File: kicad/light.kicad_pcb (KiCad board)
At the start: 4 copper layers, 58 x 40 mm, 138 parts, among them J2 USB_C_Receptacle_USB2.0_16P, J3 Barrell Jack, J4 01x04, J5 SM03B-SRSS-TB, J6 SM03B-SRSS-TB, J9 Conn_01x09_MountingPin, Q1 NMOS, Q2 NMOS, Q3 NMOS, SW1 Boot, SW3 On/Off, SW4 Mode, U1 RP2350A-QFN60, U10 MAX6816, U2 TPS5405DR, U3 W25Q128JVS, U4 LBEE5KL1YN-814, U5 TPS2115ADRBR, U6 TPS2115ADRBR, U7 HDC1080, U8 MAX6816, U9 MAX6816, Y1 ABM8-272-T3

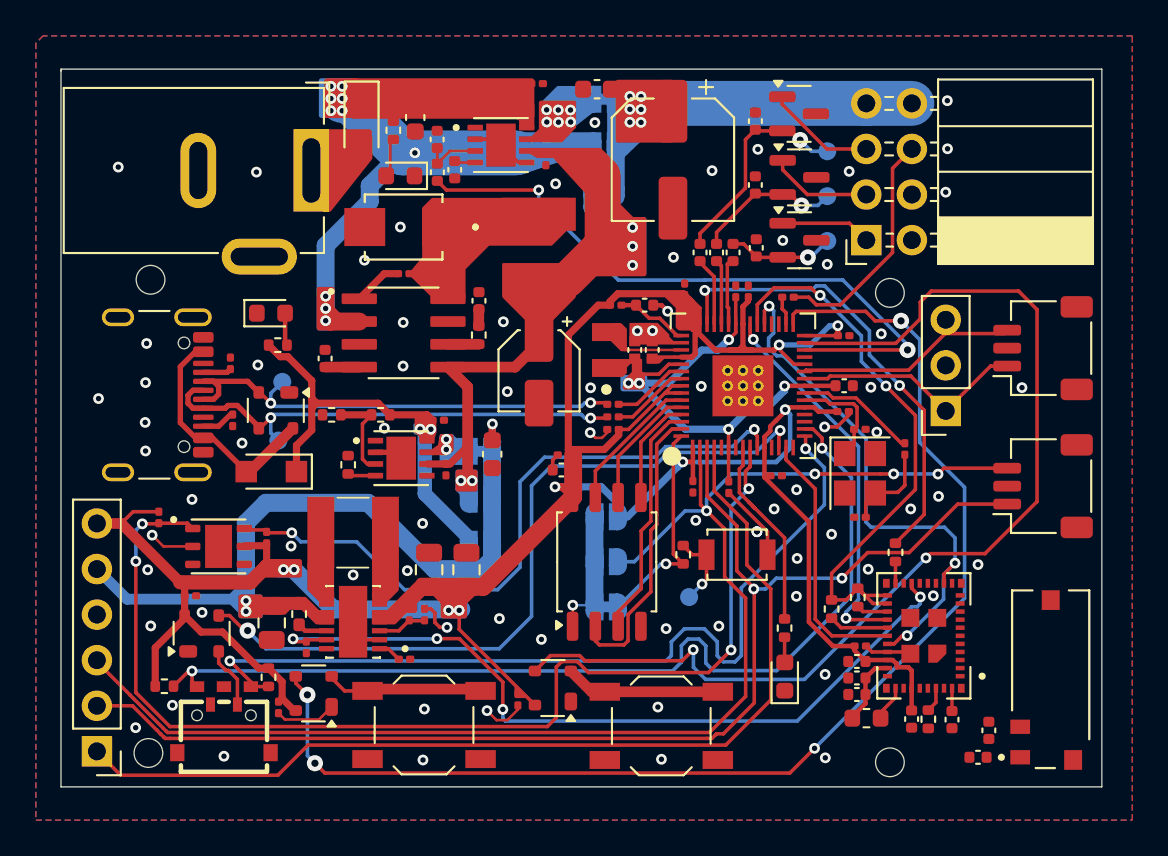
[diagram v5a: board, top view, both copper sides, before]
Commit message: make corners rounded
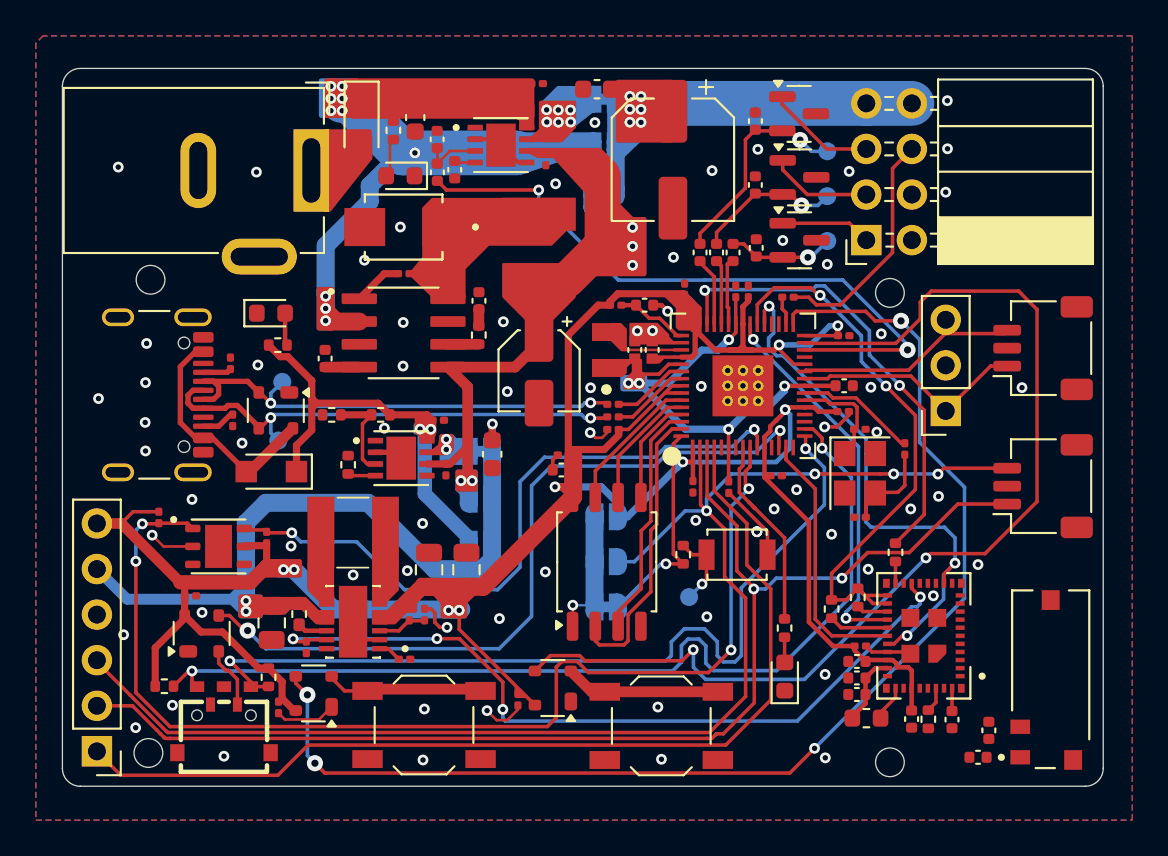
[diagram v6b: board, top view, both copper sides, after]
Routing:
- net GND: vias 76 -> 72
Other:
- outline, holes or cut-outs redrawn
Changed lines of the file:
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@@
 		(net 40)
 	)
+	(gr_rect
+		(start 125.58 77.49)
+		(end 183.58 117.49)
+		(stroke
+			(width 0.1)
+			(type default)
+		)
+		(fill no)
+		(layer "Cmts.User")
+	)
 	(gr_line
-		(start 125.51 77.48)
-		(end 125.51 77.58)
+		(start 183.587107 116.442893)
+		(end 183.587107 78.442893)
+		(stroke
+			(width 0.0381)
+			(type solid)
+		)
+		(layer "Edge.Cuts")
+	)
+	(gr_arc
+		(start 182.587107 77.442893)
+		(mid 183.294214 77.735786)
+		(end 183.587107 78.442893)
 		(stroke
 			(width 0.0381)
@@
 		(layer "Edge.Cuts")
 	)
-	(gr_line
-		(start 125.51 117.48)
-		(end 183.51 117.48)
+	(gr_arc
+		(start 183.587107 116.442893)
+		(mid 183.294214 117.15)
+		(end 182.587107 117.442893)
 		(stroke
 			(width 0.0381)
@@
 		(layer "Edge.Cuts")
 	)
-	(gr_line
-		(start 183.51 117.48)
-		(end 183.51 77.48)
+	(gr_arc
+		(start 126.587107 117.442893)
+		(mid 125.88 117.15)
+		(end 125.587107 116.442893)
 		(stroke
 			(width 0.0381)
@@
 		(layer "Edge.Cuts")
 	)
-	(gr_line
-		(start 125.51 77.58)
-		(end 125.51 117.48)
+	(gr_arc
+		(start 125.587107 78.442893)
+		(mid 125.88 77.735786)
+		(end 126.587107 77.442893)
 		(stroke
 			(width 0.0381)
@@
 	)
 	(gr_line
-		(start 183.51 77.48)
-		(end 125.51 77.48)
+		(start 126.587107 77.442893)
+		(end 182.587107 77.442893)
 		(stroke
 			(width 0.0381)
-			(type default)
+			(type solid)
+		)
+		(layer "Edge.Cuts")
+	)
+	(gr_line
+		(start 125.587107 116.442893)
+		(end 125.587107 78.442893)
+		(stroke
+			(width 0.0381)
+			(type solid)
+		)
+		(layer "Edge.Cuts")
+	)
+	(gr_line
+		(start 126.587107 117.442893)
+		(end 182.587107 117.442893)
+		(stroke
+			(width 0.0381)
+			(type solid)
 		)
 		(layer "Edge.Cuts")
@@
 	)
 	(via
+		(at 129 109)
+		(size 0.6)
+		(drill 0.3)
+		(layers "F.Cu" "B.Cu")
+		(free yes)
+		(net 2)
+	)
+	(via
 		(at 168.21 88.36)
 		(size 0.6)
@@
 	)
 	(via
-		(at 159.23 108.66)
-		(size 0.6)
-		(drill 0.3)
-		(layers "F.Cu" "B.Cu")
-		(free yes)
-		(net 2)
-	)
-	(via
 		(at 159.64 87.97)
 		(size 0.6)
@@
 	)
 	(via
-		(at 130.34 105.38)
-		(size 0.6)
-		(drill 0.3)
-		(layers "F.Cu" "B.Cu")
-		(free yes)
-		(net 2)
-	)
-	(via
 		(at 166.5 100.92)
 		(size 0.6)
@@
 	)
 	(via
-		(at 152.28 109.26)
+		(at 152.5 105.5)
 		(size 0.6)
 		(drill 0.3)
@@
 	)
 	(via
-		(at 130.51 108.51)
-		(size 0.6)
-		(drill 0.3)
-		(layers "F.Cu" "B.Cu")
-		(free yes)
-		(net 2)
-	)
-	(via
 		(at 168.09 111.21)
 		(size 0.6)
@@
 	)
 	(via
-		(at 162.17 108.52)
+		(at 161.5 108)
 		(size 0.6)
 		(drill 0.3)
@@
 	)
 	(via
-		(at 166.53 104.75)
-		(size 0.6)
-		(drill 0.3)
-		(layers "F.Cu" "B.Cu")
-		(net 2)
-	)
-	(via
 		(at 134.59 115.77)
 		(size 0.6)
@@
 	)
 	(via
-		(at 166.49 106.86)
-		(size 0.6)
-		(drill 0.3)
-		(layers "F.Cu" "B.Cu")
-		(net 2)
-	)
-	(via
 		(at 168.1 115.86)
 		(size 0.6)
@@
 		)
 	)
+	(group ""
+		(members "102964ff-ee64-426b-9564-4952c51b28c8" "81bc55f4-4432-43aa-b915-c5409ed54d11"
+			"9dac1478-53c0-4cff-8b24-059896084179" "b48257df-6c3c-44be-9981-5590594922c7"
+			"c21242df-c8e2-4d62-ac48-eb1d839e7cd5" "d5ae6d61-164b-4409-8b88-155d893a3e06"
+			"d8761f5b-b9b9-45ec-a9cf-15a7271da87b" "da0cc3e7-fb78-43c6-bea0-938829d52a9e"
+		)
+	)

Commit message: route antenna!!! oficially routed the hole board; also solved remaining DRC errors
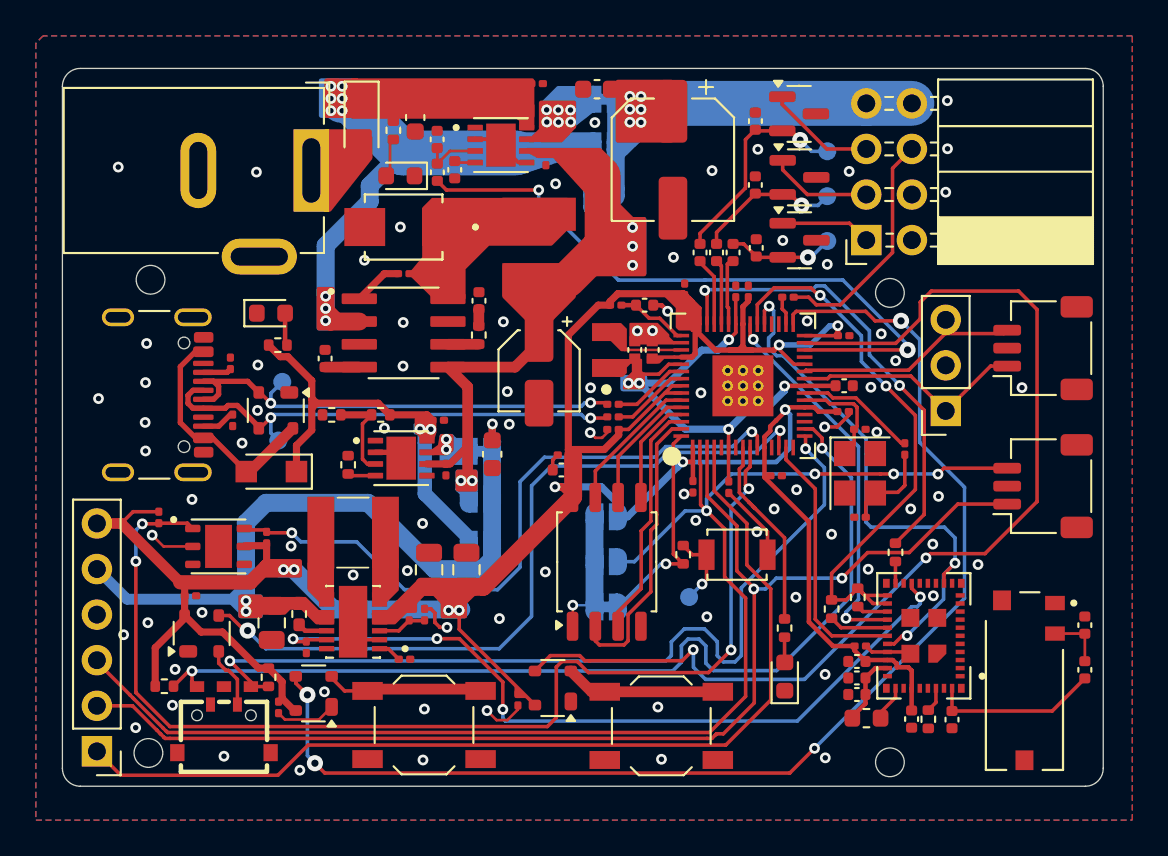
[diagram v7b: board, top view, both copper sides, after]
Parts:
- moved C44 7.94 mm to (182.6, 108.5)
- moved C31 7.69 mm to (182.6, 111.0), turned to 90 degrees
- moved AE1 1.47 mm to (179.2, 111.6), turned to 0 degrees
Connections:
- AE1 pad 1: Net-(AE1-A) -> GND
- AE1 pad 2: (no net) -> Net-(AE1-RF_Feed)
- C31 pad 2: Net-(AE1-A) -> Net-(AE1-RF_Feed)
- C44 pad 1: Net-(AE1-A) -> Net-(AE1-RF_Feed)
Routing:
- net GND: track 29.1 -> 50.9 mm, vias 72 -> 82
- net Net-(U4-ANT): track 1.27 -> 9.42 mm
- net Net-(AE1-RF_Feed): track 0.00 -> 3.20 mm
- net +12V: vias 10 -> 9
